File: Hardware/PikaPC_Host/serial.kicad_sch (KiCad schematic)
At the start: 10 parts, among them J1 DE9_Pins_MountingHoles, U1 PPC403GA, U4 GD75232N, Y2 7M3728

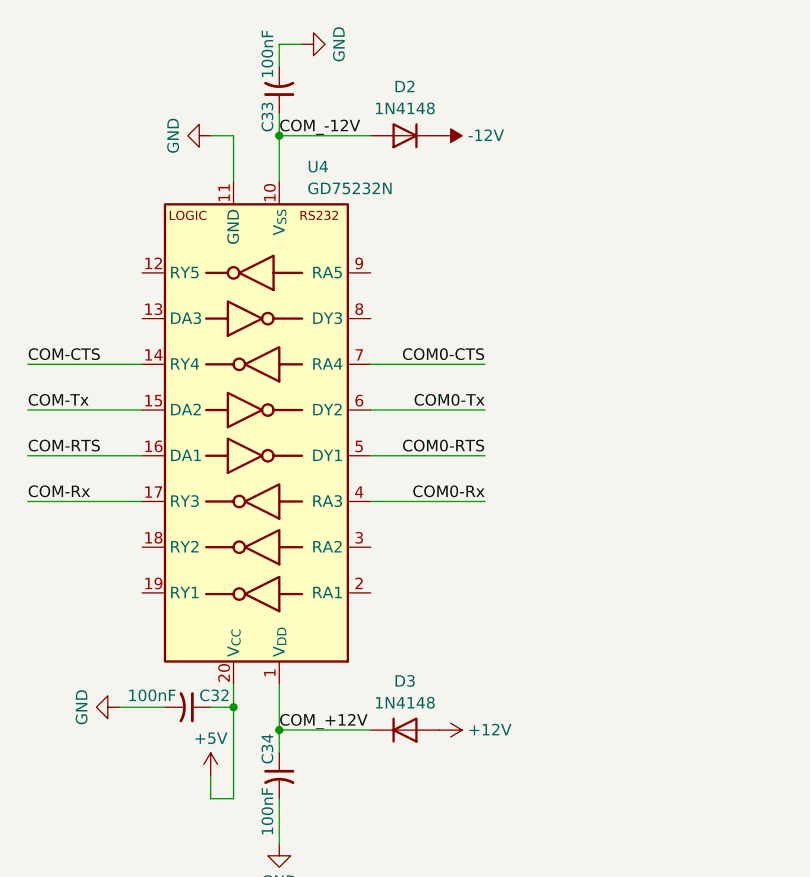
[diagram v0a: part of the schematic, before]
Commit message: Annotate & prep for output - Host & KBC
add gerber output to gitignore
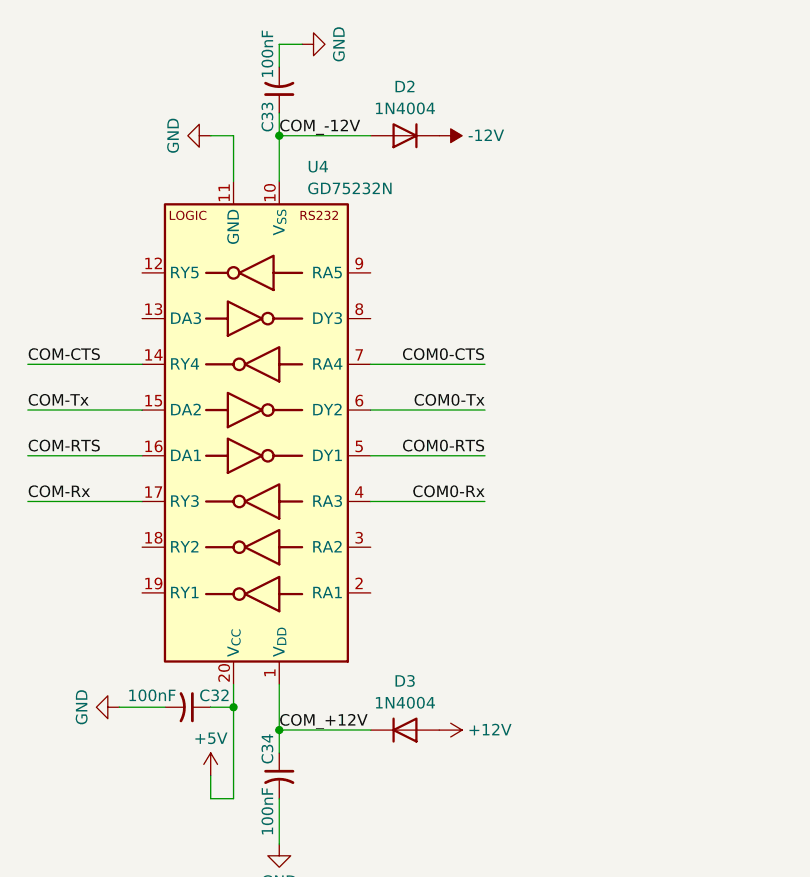
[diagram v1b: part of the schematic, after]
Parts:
- C31, C32, C33, C34: Mouser (none) -> 187-CL21B104KACNNNC
- D2, D3: value 1N4148 -> 1N4004; footprint Diode_THT:D_DO-35_SOD27_P7.62mm_Horizontal -> Diode_THT:D_DO-41_SOD81_P7.62mm_Horizontal; Mouser (none) -> 750-1N4004-G
- U4: Mouser (none) -> 595-GD75232N
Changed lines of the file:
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@@
+			)
+		)
+		(property "Mouser" "187-CL21B104KACNNNC"
+			(at 129.54 142.24 90)
+			(effects
+				(font
+					(size 1.27 1.27)
+				)
+				(hide yes)
 			)
 		)
@@
 			)
 		)
-		(property "Value" "1N4148"
+		(property "Value" "1N4004"
 			(at 143.51 134.1698 0)
 			(effects
@@
 			)
 		)
-		(property "Footprint" "Diode_THT:D_DO-35_SOD27_P7.62mm_Horizontal"
+		(property "Footprint" "Diode_THT:D_DO-41_SOD81_P7.62mm_Horizontal"
 			(at 143.51 137.16 0)
 			(effects
@@
 			)
 		)
-		(property "Datasheet" "https://assets.nexperia.com/documents/data-sheet/1N4148_1N4448.pdf"
+		(property "Datasheet" ""
 			(at 143.51 137.16 0)
 			(effects
@@
 		)
 		(property "Sim.Pins" "1=K 2=A"
+			(at 143.51 137.16 0)
+			(effects
+				(font
+					(size 1.27 1.27)
+				)
+				(hide yes)
+			)
+		)
+		(property "Mouser" "750-1N4004-G "
 			(at 143.51 137.16 0)
 			(effects
@@
 		(property "Description" ""
 			(at 119.38 134.62 0)
+			(effects
+				(font
+					(size 1.27 1.27)
+				)
+				(hide yes)
+			)
+		)
+		(property "Mouser" "187-CL21B104KACNNNC"
+			(at 119.38 134.62 90)
 			(effects
 				(font
@@
 			)
 		)
-		(property "Value" "1N4148"
+		(property "Value" "1N4004"
 			(at 143.51 68.1298 0)
 			(effects
@@
 			)
 		)
-		(property "Footprint" "Diode_THT:D_DO-35_SOD27_P7.62mm_Horizontal"
+		(property "Footprint" "Diode_THT:D_DO-41_SOD81_P7.62mm_Horizontal"
 			(at 143.51 71.12 0)
 			(effects
@@
 			)
 		)
-		(property "Datasheet" "https://assets.nexperia.com/documents/data-sheet/1N4148_1N4448.pdf"
+		(property "Datasheet" ""
 			(at 143.51 71.12 0)
 			(effects
@@
 		)
 		(property "Sim.Pins" "1=K 2=A"
+			(at 143.51 71.12 0)
+			(effects
+				(font
+					(size 1.27 1.27)
+				)
+				(hide yes)
+			)
+		)
+		(property "Mouser" "750-1N4004-G "
 			(at 143.51 71.12 0)
 			(effects
@@
 			)
 		)
+		(property "Mouser" "595-GD75232N "
+			(at 127 104.14 0)
+			(effects
+				(font
+					(size 1.27 1.27)
+				)
+				(hide yes)
+			)
+		)
 		(pin "4"
 		)
@@
 			)
 		)
+		(property "Mouser" "187-CL21B104KACNNNC"
+			(at 129.54 66.04 90)
+			(effects
+				(font
+					(size 1.27 1.27)
+				)
+				(hide yes)
+			)
+		)
 		(pin "2"
 		)
@@
 			(effects
 				(font
+					(size 1.27 1.27)
+				)
+				(hide yes)
+			)
+		)
+		(property "Mouser" "187-CL21B104KACNNNC"
+			(at 39.37 127 90)
+			(effects
+				(font
